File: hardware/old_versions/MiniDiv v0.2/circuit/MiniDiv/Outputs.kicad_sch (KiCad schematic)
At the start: 30 parts, among them J10 OUT_512, J11 OUT_1024, J2 OUT_2, J3 OUT_4, J4 OUT_8, J5 OUT_16, J6 OUT_32, J7 OUT_64, J8 OUT_128, J9 OUT_256

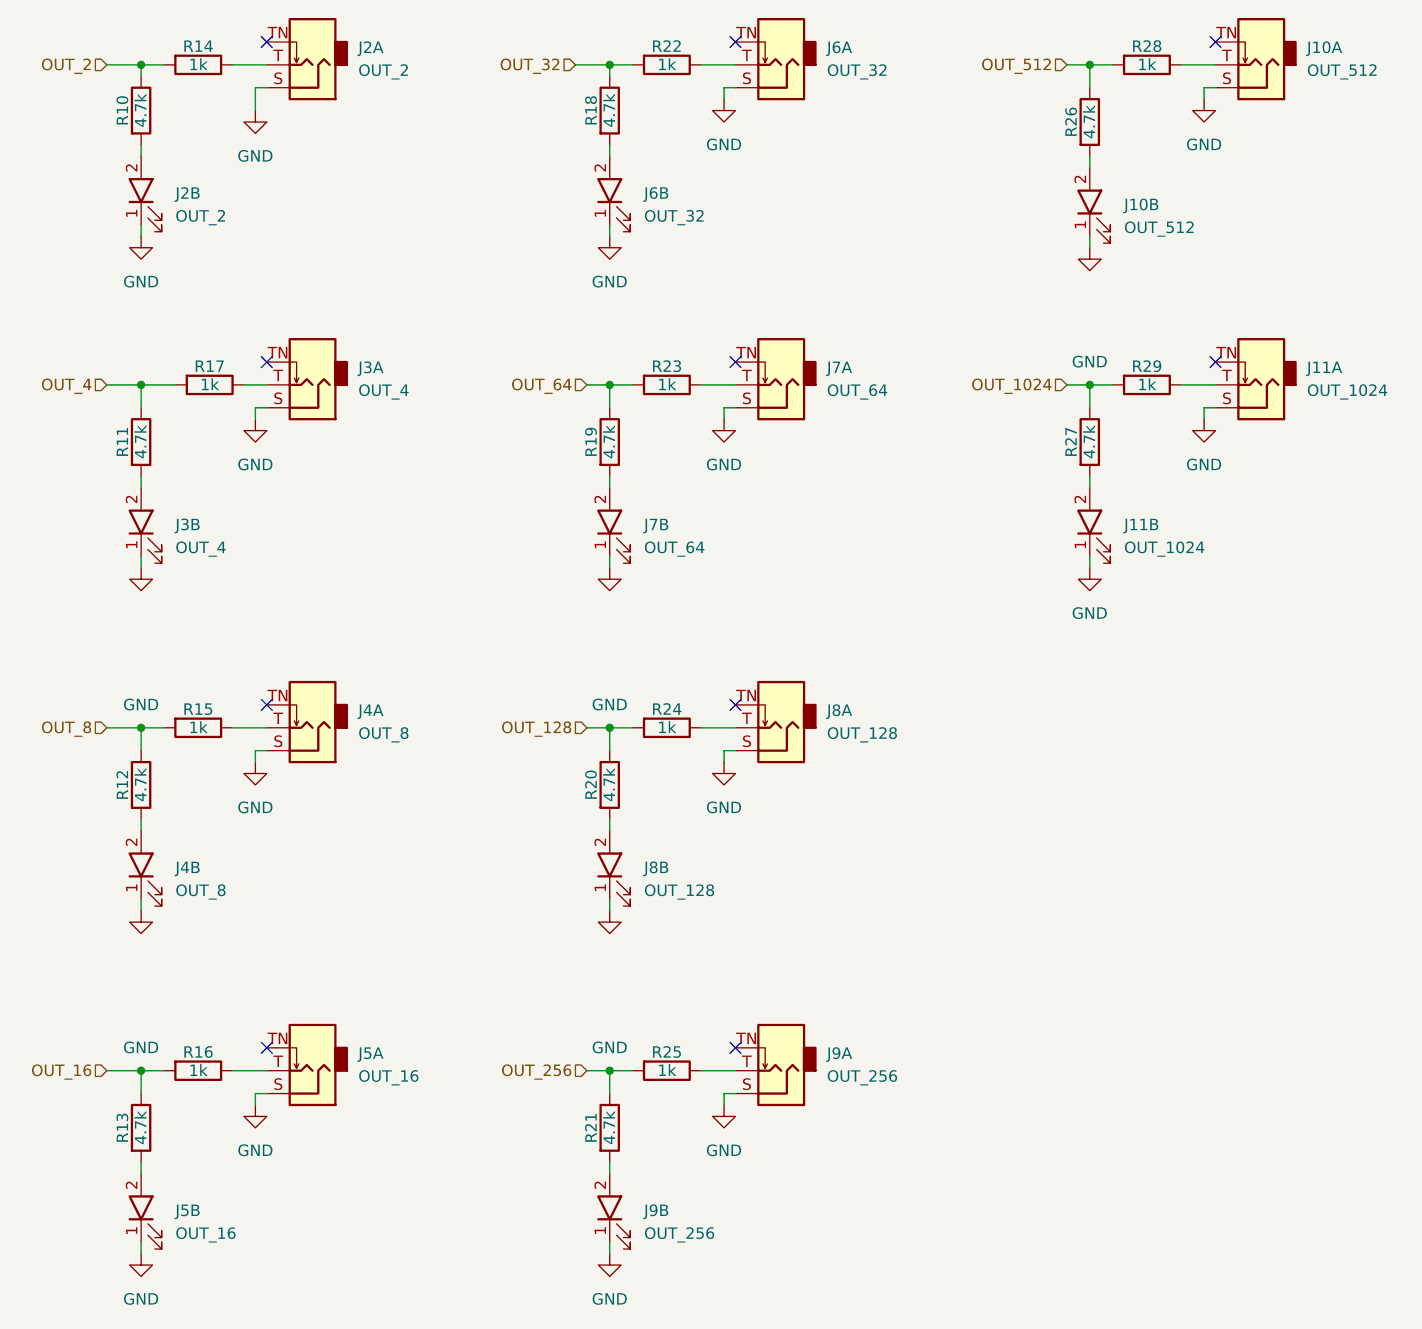
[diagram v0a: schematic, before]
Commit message: Fixed LED clearance issues
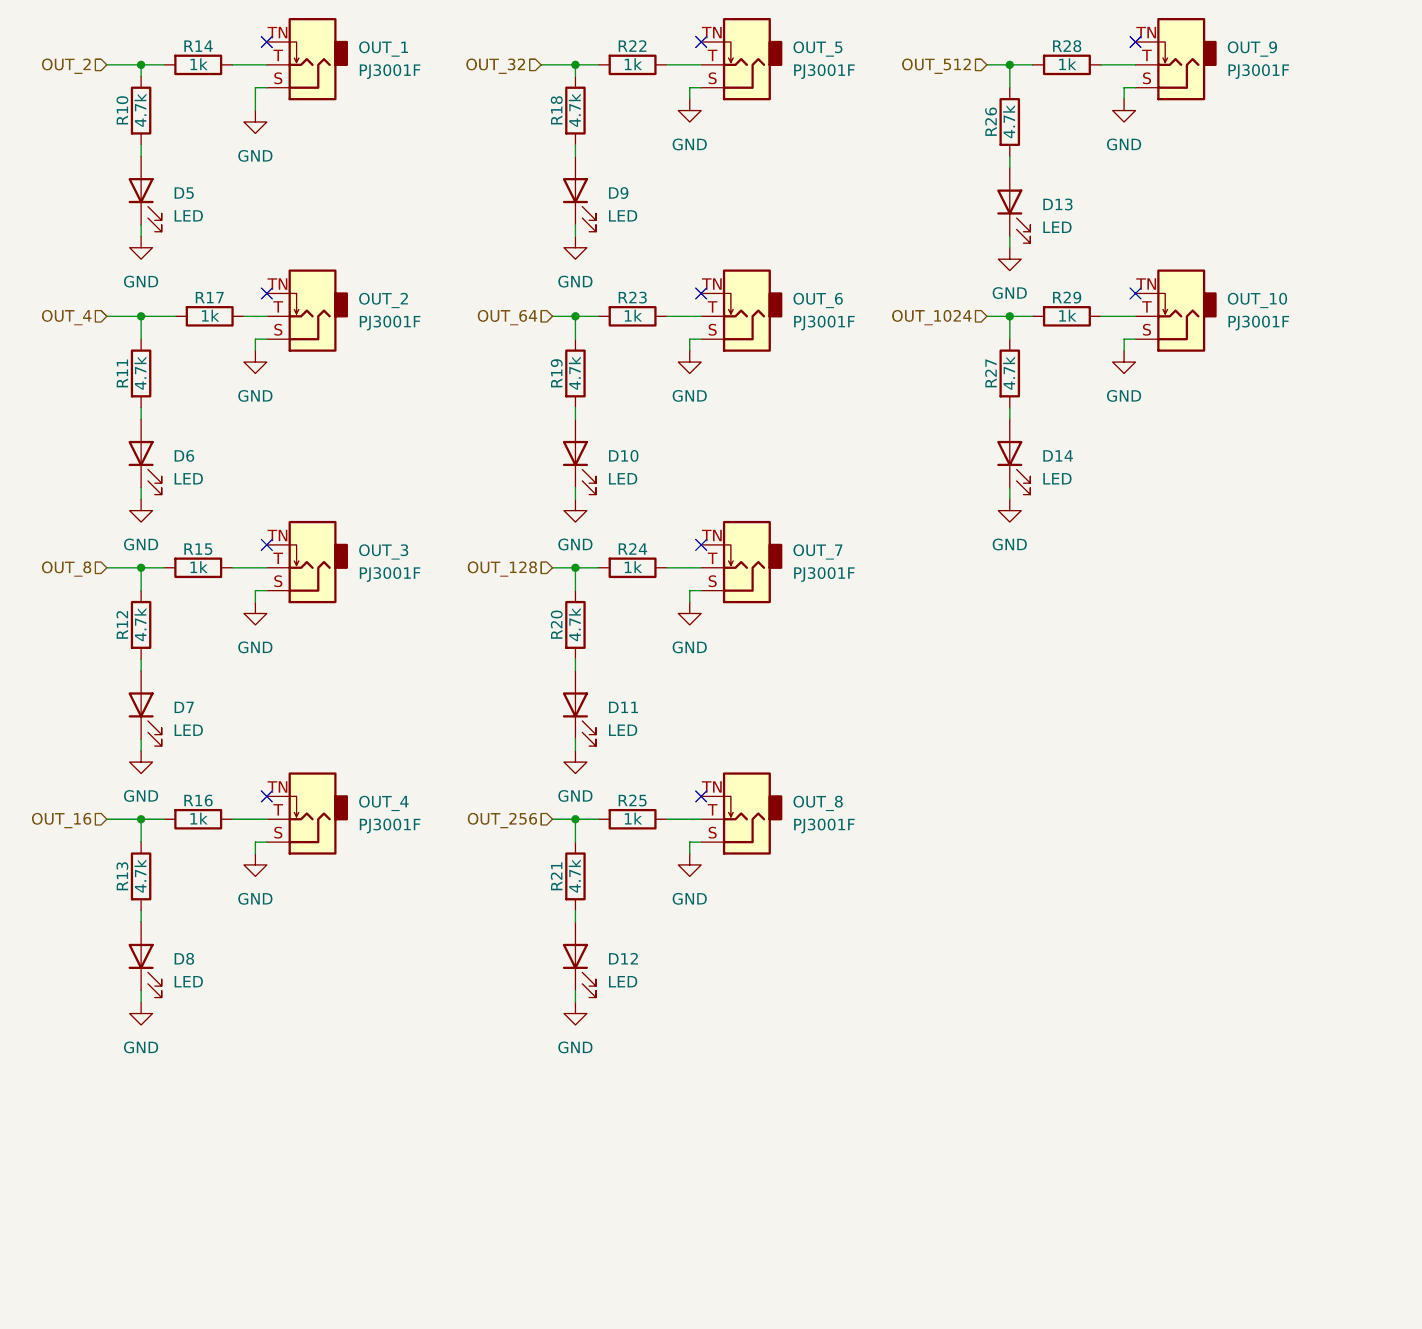
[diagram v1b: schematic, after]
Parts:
- removed J10: OUT_512, benjiaomodular:AudioJack_PJ3001F_0805LED, symbol benjiaomodular:PJ3001F_LED
- removed J11: OUT_1024, benjiaomodular:AudioJack_PJ3001F_0805LED, symbol benjiaomodular:PJ3001F_LED
- removed J2: OUT_2, benjiaomodular:AudioJack_PJ3001F_0805LED, symbol benjiaomodular:PJ3001F_LED
- removed J3: OUT_4, benjiaomodular:AudioJack_PJ3001F_0805LED, symbol benjiaomodular:PJ3001F_LED
- removed J4: OUT_8, benjiaomodular:AudioJack_PJ3001F_0805LED, symbol benjiaomodular:PJ3001F_LED
- removed J5: OUT_16, benjiaomodular:AudioJack_PJ3001F_0805LED, symbol benjiaomodular:PJ3001F_LED
- removed J6: OUT_32, benjiaomodular:AudioJack_PJ3001F_0805LED, symbol benjiaomodular:PJ3001F_LED
- removed J7: OUT_64, benjiaomodular:AudioJack_PJ3001F_0805LED, symbol benjiaomodular:PJ3001F_LED
- removed J8: OUT_128, benjiaomodular:AudioJack_PJ3001F_0805LED, symbol benjiaomodular:PJ3001F_LED
- removed J9: OUT_256, benjiaomodular:AudioJack_PJ3001F_0805LED, symbol benjiaomodular:PJ3001F_LED
- added D10, D11, D12, D13, D14, D5, D6, D7, D8, D9: LED, LED_SMD:LED_0805_2012Metric, symbol Device:LED
- added OUT_1, OUT_10, OUT_2, OUT_3, OUT_4, OUT_5, OUT_6, OUT_7, OUT_8, OUT_9: PJ3001F, benjiaomodular:AudioJack_3.5mm, symbol benjiaomodular:PJ3001F
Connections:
- net GND: now also D10.1 (K), D11.1 (K), D12.1 (K), D13.1 (K), D14.1 (K), D5.1 (K), D6.1 (K), D7.1 (K), D8.1 (K), D9.1 (K), OUT_1.S, OUT_10.S, OUT_2.S, OUT_3.S, OUT_4.S, OUT_5.S, OUT_6.S, OUT_7.S, OUT_8.S, OUT_9.S
- net at R10.2: now also D5.2 (A)
- net at R20.2: now also D11.2 (A)
- net at R11.2: now also D6.2 (A)
- net at R16.1: now also OUT_4.T
- net at R19.2: now also D10.2 (A)
- net at R24.1: now also OUT_7.T
- net at R13.2: now also D8.2 (A)
- net at R23.1: now also OUT_6.T
- net at R29.1: now also OUT_10.T
- net at R26.2: now also D13.2 (A)
- net at R28.1: now also OUT_9.T
- net at R22.1: now also OUT_5.T
- net at R27.2: now also D14.2 (A)
- net at R21.2: now also D12.2 (A)
- net at R15.1: now also OUT_3.T
- net at R25.1: now also OUT_8.T
- net at R18.2: now also D9.2 (A)
- net at R12.2: now also D7.2 (A)
- net at R17.1: now also OUT_2.T
- net at R14.1: now also OUT_1.T
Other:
- moved on the sheet: R11, R12, R13, R15, R16, R17, R18, R19, R20, R21, R22, R23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
